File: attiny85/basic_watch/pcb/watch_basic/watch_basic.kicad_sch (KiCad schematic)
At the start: 22 parts, among them J2 USB C, J3 Programmer, P1 JST_LIPO, SW1 Wake, SW2 Select, SW3 Set, SW4 Reset, U1 ATTINY85, U2 MCP73831-2-OT, U3 SSD1306_OLED_Display_128x64

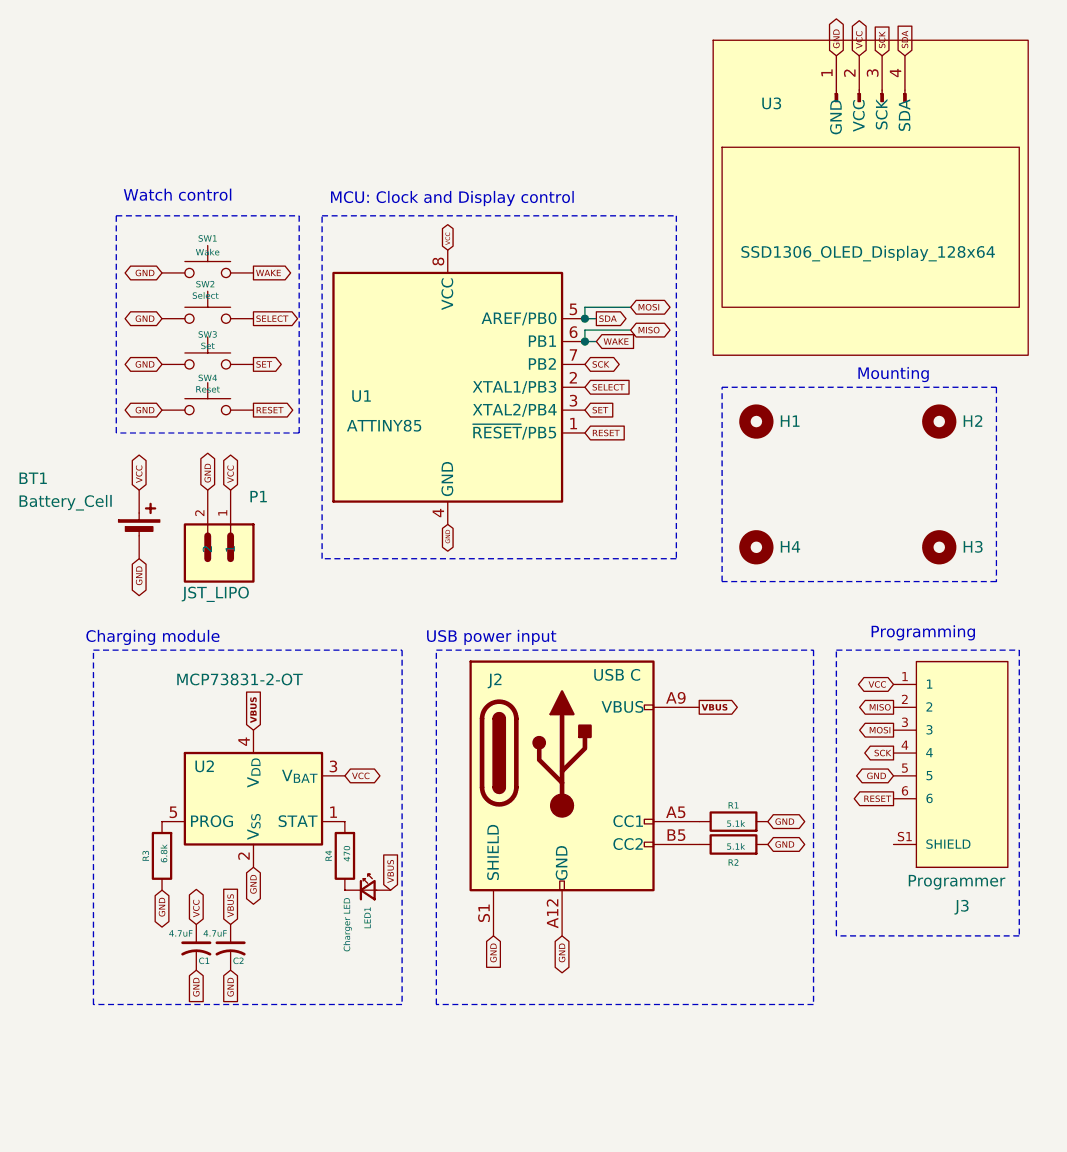
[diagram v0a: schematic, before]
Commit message: split by basic and charger versions
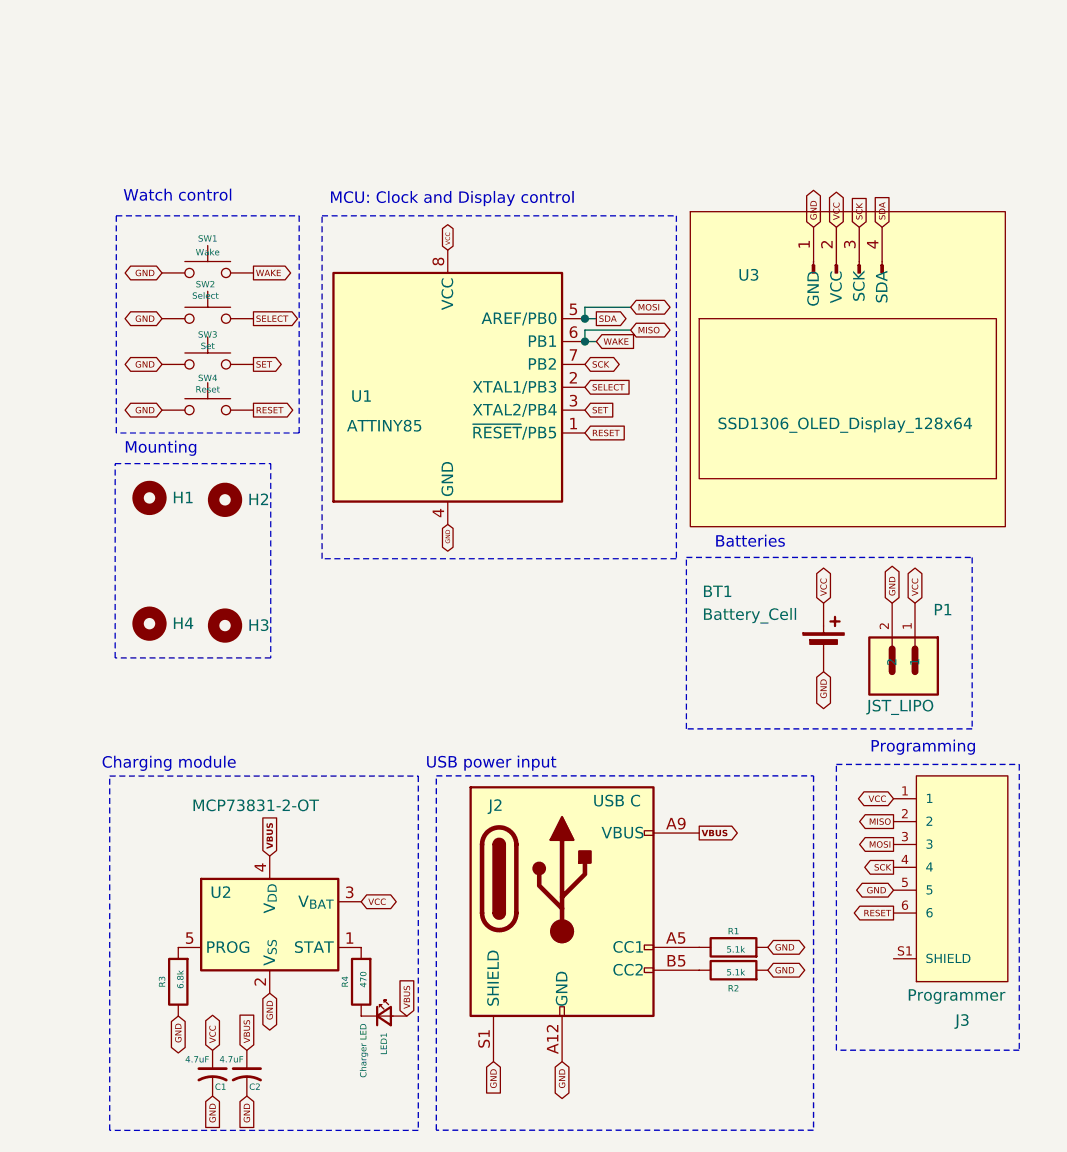
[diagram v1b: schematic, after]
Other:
- note added: "Batteries"
- moved on the sheet: BT1, C1, C2, H1, H2, H3, H4, J2, J3, LED1, P1, R1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
